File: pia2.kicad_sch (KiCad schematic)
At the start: 42 parts, among them IC25 LM393P, IC31 74LS02N, IC34 MC14050BCP, IC35 MC6821, IC9 MC6821

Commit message: move to samx4
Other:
- company: (none) -> Dragon Data
- title: (none) -> Dragon 32 CPU UK PAL
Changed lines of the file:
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@@
   (paper "A3")
   (title_block
+    (title "Dragon 32 CPU UK PAL")
     (date "2023-05-25")
     (rev "3.0")
+    (company "Dragon Data")
+    (comment 1 "Modified by Julian Brown")
+    (comment 2 "SAMx4 by Ciaran Anscomb")
   )
   (junction (at 44.45 171.45) (diameter 0) (color 0 0 0 0)

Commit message: rework board
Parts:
- removed IC35, IC9: MC6821, Package_DIP:DIP-40_W15.24mm, symbol Motorola PIA:MC6821
- removed R57: 20K 1%, Resistor_THT:R_Axial_DIN0207_L6.3mm_D2.5mm_P10.16mm_Horizontal, symbol Device:R_Small
- removed R58: 80K6 1%, Resistor_THT:R_Axial_DIN0207_L6.3mm_D2.5mm_P10.16mm_Horizontal, symbol Device:R_Small
- removed R59: 160K 1%, Resistor_THT:R_Axial_DIN0207_L6.3mm_D2.5mm_P10.16mm_Horizontal, symbol Device:R_Small
- removed R60: 330K 1%, Resistor_THT:R_Axial_DIN0207_L6.3mm_D2.5mm_P10.16mm_Horizontal, symbol Device:R_Small
- removed R61: 40K2 1%, Resistor_THT:R_Axial_DIN0207_L6.3mm_D2.5mm_P10.16mm_Horizontal, symbol Device:R_Small
- removed R62: 10K 1%, Resistor_THT:R_Axial_DIN0207_L6.3mm_D2.5mm_P10.16mm_Horizontal, symbol Device:R_Small
- removed R64: 100K, Resistor_THT:R_Axial_DIN0207_L6.3mm_D2.5mm_P10.16mm_Horizontal, symbol Device:R_Small
- added J5: 6-bit DAC, Connector_PinSocket_2.54mm:PinSocket_1x08_P2.54mm_Vertical, symbol Connector_Generic:Conn_01x08
- added U5 (x2): W65C21, Package_LCC:PLCC-44_SMD-Socket, symbol Motorola PIA:W65C21
- C2, C35, C42: footprint Capacitor_THT:CP_Radial_D5.0mm_P2.50mm -> Capacitor_SMD:CP_Elec_5x5.3
- C26, C48: footprint Capacitor_THT:C_Disc_D3.0mm_W2.0mm_P2.50mm -> Capacitor_SMD:C_0805_2012Metric_Pad1.18x1.45mm_HandSolder
- C27: footprint Capacitor_THT:C_Disc_D4.3mm_W1.9mm_P5.00mm -> Capacitor_SMD:C_0805_2012Metric_Pad1.18x1.45mm_HandSolder
- C44: footprint Capacitor_THT:C_Disc_D5.0mm_W2.5mm_P5.00mm -> Capacitor_SMD:C_0805_2012Metric_Pad1.18x1.45mm_HandSolder
- D1, D2, D3, D7: footprint Diode_THT:D_DO-35_SOD27_P7.62mm_Horizontal -> Diode_SMD:D_SOD-323_HandSoldering
- IC31: value 74LS02N -> 74ACT02; footprint Package_DIP:DIP-14_W7.62mm -> Package_SO:SOIC-14_3.9x8.7mm_P1.27mm; DigiKey 296-1627-5-ND -> MC74ACT02DR2GOSCT-ND
- IC34: value MC14050BCP -> CD4050BDR; footprint Package_DIP:DIP-16_W7.62mm -> Package_SO:SOIC-16W_7.5x10.3mm_P1.27mm; DigiKey 296-2056-ND -> 296-31503-1-ND; Note obsolete use CD4050B or convert MC14050BDG -> (none)
- R16, R32: footprint Resistor_THT:R_Axial_DIN0207_L6.3mm_D2.5mm_P2.54mm_Vertical -> Resistor_SMD:R_0805_2012Metric_Pad1.20x1.40mm_HandSolder
- R29, R38, R45, R46, R47, R48, R49, R50, R51, R52, R56, R63: footprint Resistor_THT:R_Axial_DIN0207_L6.3mm_D2.5mm_P10.16mm_Horizontal -> Resistor_SMD:R_0805_2012Metric_Pad1.20x1.40mm_HandSolder
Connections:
- net +5V: now also J5.1 (Pin_1), U5.21 (VCC), U5.21 (VCC), U5.24 (CS0), U5.24 (CS0), U5.26 (CS1), U5.26 (CS1)
- net 6bit D/A: now also J5.8 (Pin_8)
- net A0: now also U5.39 (RS0), U5.39 (RS0)
- net A1: now also U5.38 (RS1), U5.38 (RS1)
- net Alpha: now also U5.11 (PB0)
- net CART: now also U5.19 (CB1)
- net CB2: now also U5.20 (CB2)
- net CSS: now also U5.14 (PB3)
- net D0: now also U5.36 (D0), U5.36 (D0)
- net D1: now also U5.35 (D1), U5.35 (D1)
- net D2: now also U5.34 (D2), U5.34 (D2)
- net D3: now also U5.33 (D3), U5.33 (D3)
- net D4: now also U5.32 (D4), U5.32 (D4)
- net D5: now also U5.31 (D5), U5.31 (D5)
- net D6: now also U5.30 (D6), U5.30 (D6)
- net D7: now also U5.29 (D7), U5.29 (D7)
- net DAC0: now also J5.2 (Pin_2)
- net DAC1: now also J5.3 (Pin_3)
- net DAC2: now also J5.4 (Pin_4)
- net DAC3: now also J5.5 (Pin_5)
- net DAC4: now also J5.6 (Pin_6)
- net DAC5: now also J5.7 (Pin_7)
- net DC0: now also U5.3 (PA0)
- net DC1: now also U5.4 (PA1)
- net DC2: now also U5.5 (PA2)
- net DC3: now also U5.6 (PA3)
- net DC4: now also U5.7 (PA4)
- net DC5: now also U5.8 (PA5)
- net DC6: now also U5.9 (PA6)
- net DC7: now also U5.10 (PA7)
- net E: now also U5.28 (E), U5.28 (E)
- net GM0: now also U5.15 (PB4)
- net GM1: now also U5.16 (PB5)
- net GM2: now also U5.17 (PB6)
- net GND: now also U5.1 (VSS), U5.1 (VSS)
- net Inverse: now also U5.12 (PB1)
- net MEM-SIZE: now also U5.13 (PB2)
- net MOTOR: now also U5.43 (CA2)
- net P1a: now also U5.25 (~{CS2})
- net P1b: now also U5.25 (~{CS2})
- net PC0: now also U5.3 (PA0)
- net PIADAC0: now also U5.5 (PA2)
- net PIADAC1: now also U5.6 (PA3)
- net PIADAC2: now also U5.7 (PA4)
- net PIADAC3: now also U5.8 (PA5)
- net PIADAC4: now also U5.9 (PA6)
- net PIADAC5: now also U5.10 (PA7)
- net RC: now also U5.15 (PB4)
- net RClk: now also U5.14 (PB3)
- net R/~{W}: now also U5.23 (R/~{W}), U5.23 (R/~{W})
- net ~{ACK}: now also U5.44 (CA1)
- net ~{A}/G: now also U5.18 (PB7)
- net ~{BUSY}: now also U5.11 (PB0)
- net ~{FIRQ}: now also U5.41 (~{IRQB}), U5.41 (~{IRQB}), U5.42 (~{IRQA}), U5.42 (~{IRQA})
- net ~{RES}: now also U5.37 (~{RESET}), U5.37 (~{RESET})
- net ~{SelInv}: now also U5.13 (PB2)
- net at R56.2: now also U5.12 (PB1)
- net at JP2.2 (C): now also U5.4 (PA1)

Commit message: serial wiring
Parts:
- removed TR1: PN2222, Package_TO_SOT_THT:TO-92_Inline_Wide, symbol Transistor_BJT:BC141
- added TR1: PZT2222A, Package_TO_SOT_SMD:SOT-223-3_TabPin2, symbol Transistor_BJT:PZT2222A
- IC1: renamed from IC25; value LM393P -> LM393DR; footprint Package_DIP:DIP-8_W7.62mm -> Package_SO:SOP-8_3.9x4.9mm_P1.27mm; DigiKey 296-1398-5-ND -> 296-1015-1-ND
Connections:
- net Alpha: now also U5.15 (PB4); no longer U5.11 (PB0)
- net DAC1: now also IC34.12 (OUTe); no longer IC34.2 (OUTa)
- net DAC2: now also IC34.10 (OUTd); no longer IC34.4 (OUTb)
- net DAC3: now also IC34.6 (OUTc); no longer IC34.12 (OUTe)
- net DAC4: now also IC34.4 (OUTb); no longer IC34.6 (OUTc)
- net DAC5: now also IC34.2 (OUTa); no longer IC34.10 (OUTd)
- net GND: now also TR1.3 (E)
- net Inverse: now also U5.14 (PB3); no longer U5.12 (PB1)
- net PIADAC1: now also IC34.11 (INe); no longer IC34.3 (INa)
- net PIADAC2: now also IC34.9 (INd); no longer IC34.5 (INb)
- net PIADAC3: now also IC34.7 (INc); no longer IC34.11 (INe)
- net PIADAC4: now also IC34.5 (INb); no longer IC34.7 (INc)
- net PIADAC5: now also IC34.3 (INa); no longer IC34.9 (INd)
- net RC: now also U5.11 (PB0); no longer U5.15 (PB4)
- net RClk: now also U5.12 (PB1); no longer U5.14 (PB3)
- net at R32.2: now also TR1.1 (B)
- net at D1.2 (A), RL1.1: now also TR1.2 (C)

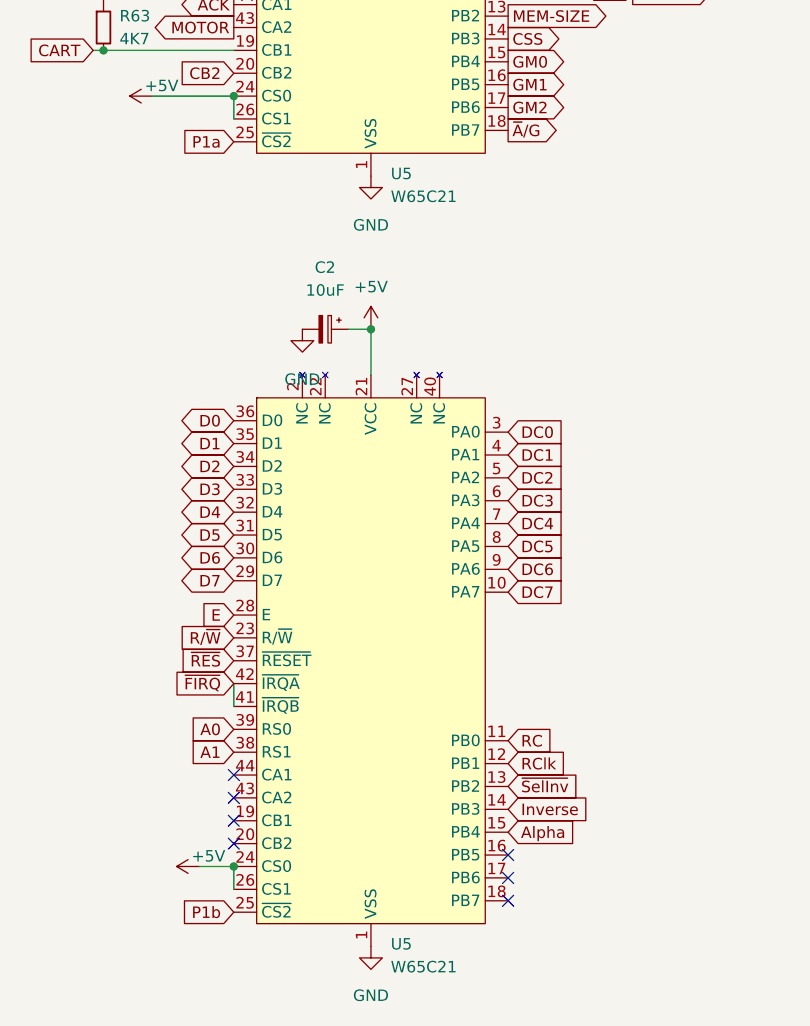
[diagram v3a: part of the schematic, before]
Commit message: fix OE timing on SRAM
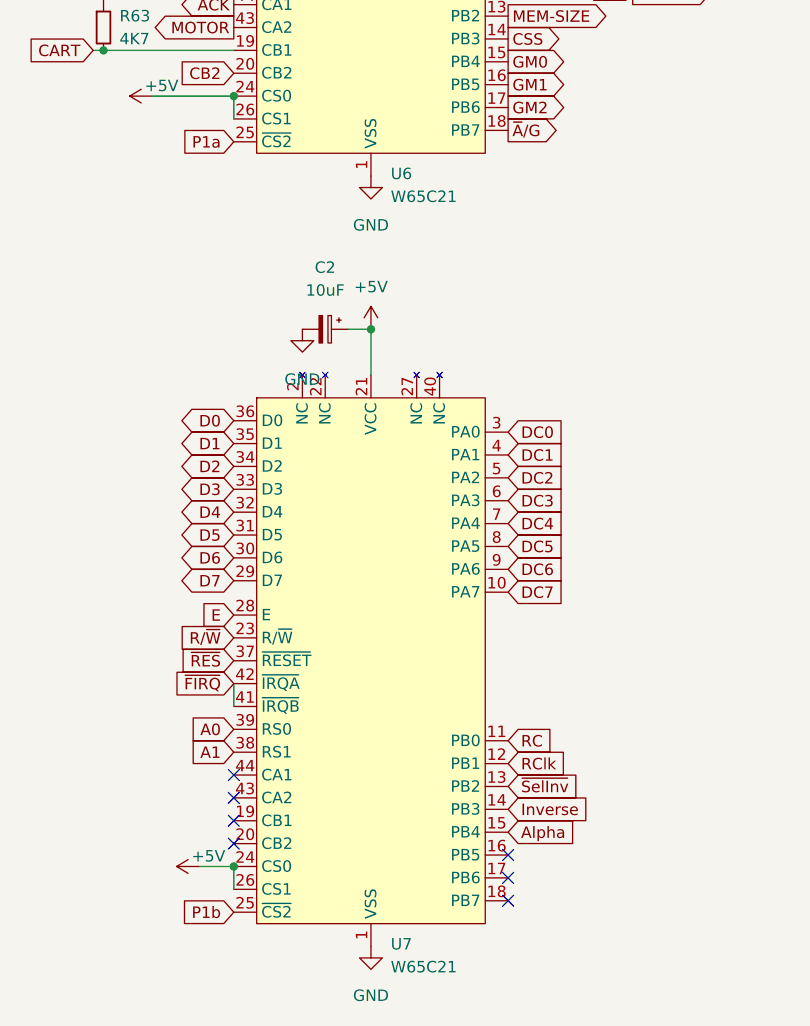
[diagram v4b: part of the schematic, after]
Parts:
- renumbered U5 to U6, U5 to U7
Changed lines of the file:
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@@
   (symbol (lib_id "Motorola PIA:W65C21") (at 59.69 64.262 0) (unit 1)
     (in_bom yes) (on_board yes) (dnp no) (fields_autoplaced)
-    (property "Reference" "U5" (at 61.8841 94.488 0)
+    (property "Reference" "U6" (at 61.8841 94.488 0)
       (effects (font (size 1.27 1.27)) (justify left))
     )
@@
     (instances
       (project "Dragon32"
-        (path "/0c3dceba-7c95-4b3d-b590-0eb581444beb/64d8d7b7-14ab-4042-9ee8-f1aec24a139c"
-          (reference "U5") (unit 1)
-        )
         (path "/0c3dceba-7c95-4b3d-b590-0eb581444beb/28dac1c2-804e-40fd-9ff5-acdb4226ab76"
           (reference "U6") (unit 1)
@@
   (symbol (lib_id "Motorola PIA:W65C21") (at 59.69 149.86 0) (unit 1)
     (in_bom yes) (on_board yes) (dnp no) (fields_autoplaced)
-    (property "Reference" "U5" (at 61.8841 180.086 0)
+    (property "Reference" "U7" (at 61.8841 180.086 0)
       (effects (font (size 1.27 1.27)) (justify left))
     )
@@
     (instances
       (project "Dragon32"
-        (path "/0c3dceba-7c95-4b3d-b590-0eb581444beb/64d8d7b7-14ab-4042-9ee8-f1aec24a139c"
-          (reference "U5") (unit 1)
-        )
         (path "/0c3dceba-7c95-4b3d-b590-0eb581444beb/28dac1c2-804e-40fd-9ff5-acdb4226ab76"
           (reference "U7") (unit 1)

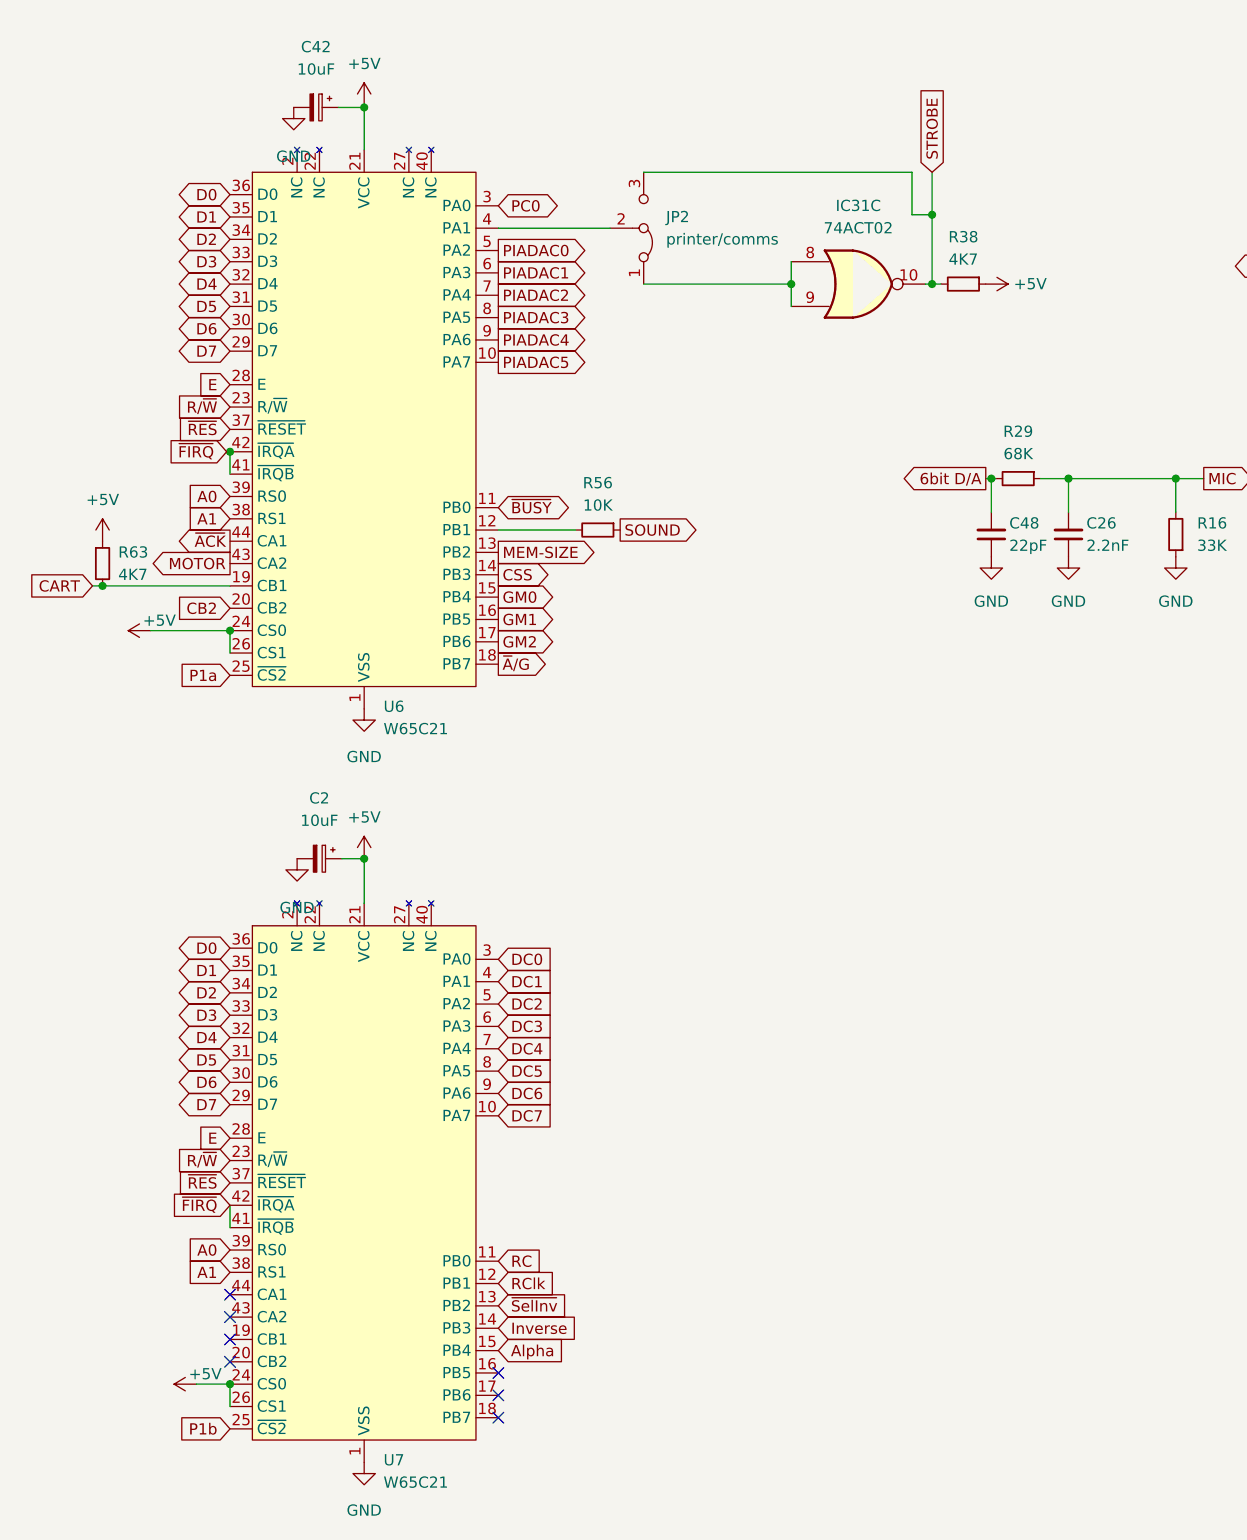
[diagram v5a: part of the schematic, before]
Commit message: switch to fpga
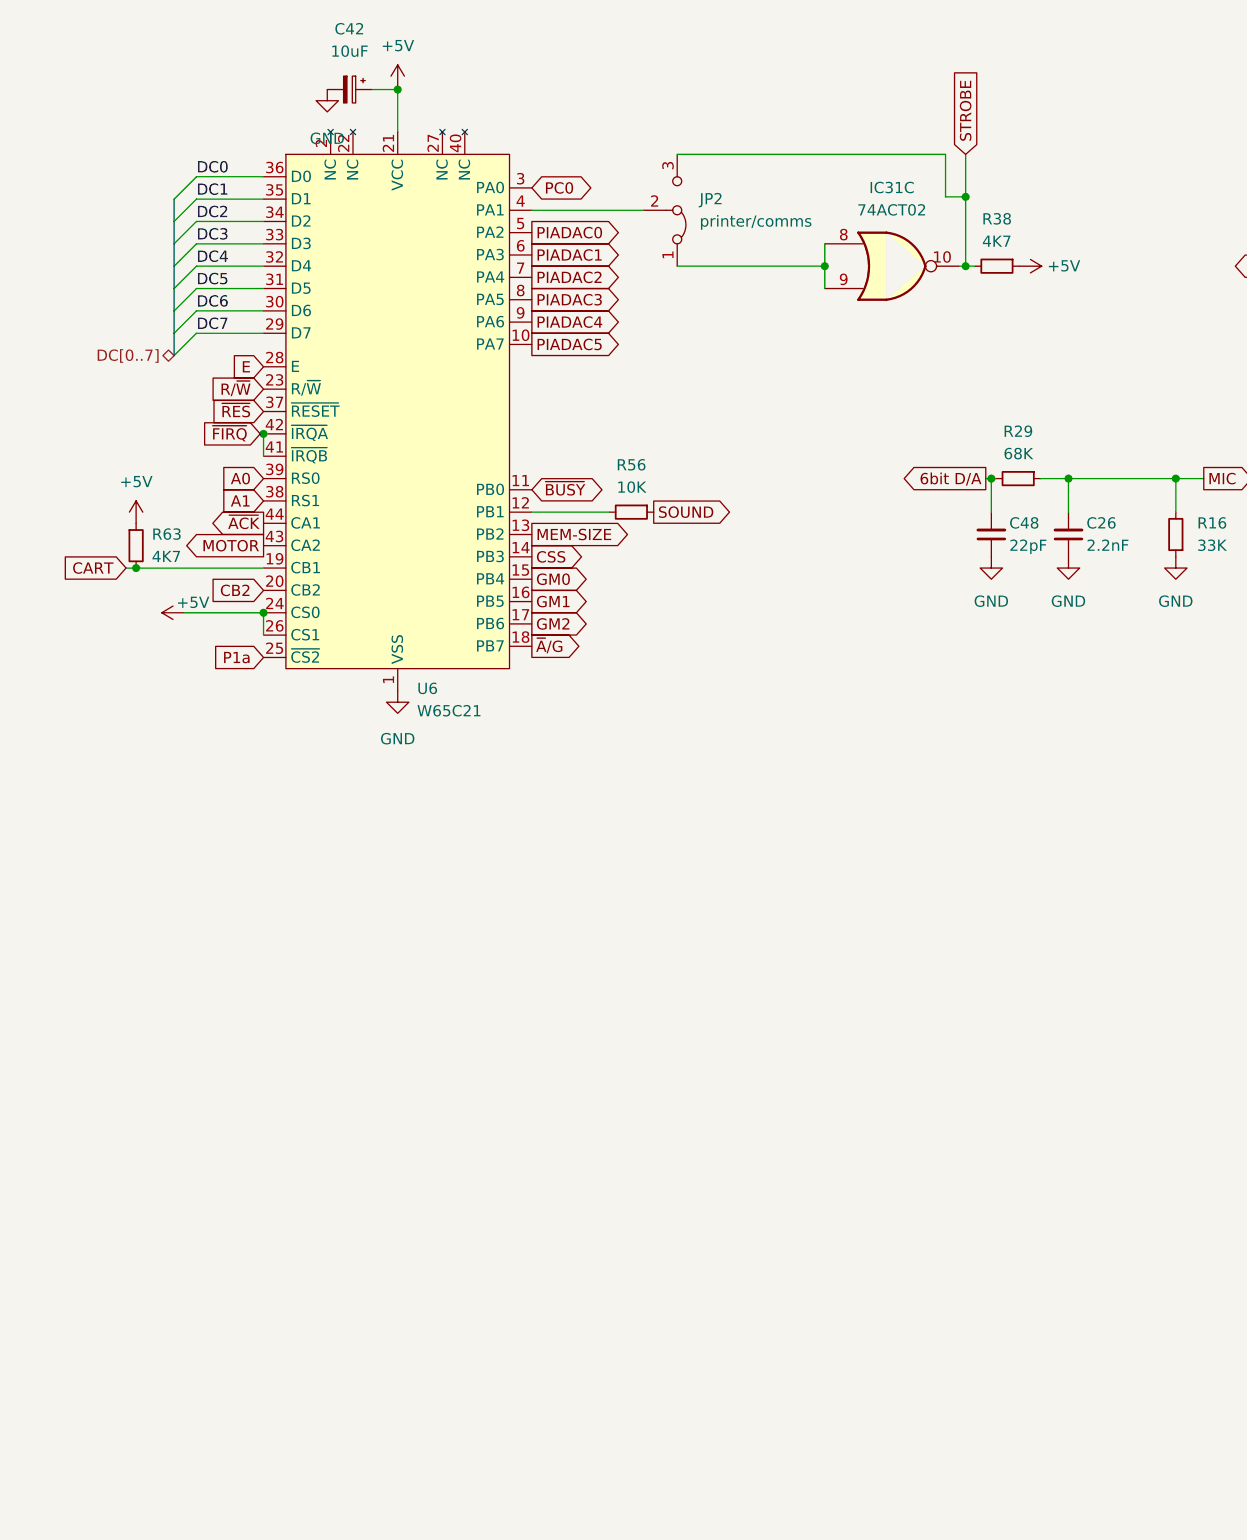
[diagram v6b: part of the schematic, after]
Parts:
- removed C2: 10uF, Capacitor_SMD:CP_Elec_5x5.3, symbol Device:C_Polarized_Small
- removed U7: W65C21, Package_LCC:PLCC-44_SMD-Socket, symbol Motorola PIA:W65C21
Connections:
- net D0 is gone; now on net DC0: U6.36 (D0)
- net D1 is gone; now on net DC1: U6.35 (D1)
- net D2 is gone; now on net DC2: U6.34 (D2)
- net D3 is gone; now on net DC3: U6.33 (D3)
- net D4 is gone; now on net DC4: U6.32 (D4)
- net D5 is gone; now on net DC5: U6.31 (D5)
- net D6 is gone; now on net DC6: U6.30 (D6)
- net D7 is gone; now on net DC7: U6.29 (D7)
- no-connect marks 8 -> 1
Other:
- moved on the sheet: C42, IC31C, JP2, R38, R56, R63, U6

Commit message: rework traces for FPGA
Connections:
- net ~{FIRQ} renamed ~{FIRQx}
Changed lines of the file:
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@@
-	)
-	(junction
-		(at 48.26 63.5)
-		(diameter 0)
-		(color 0 0 0 0)
 	)
 	(junction
@@
 		)
 	)
-	(global_label "~{FIRQ}"
-		(shape input)
-		(at 47.879 63.5 180)
-		(fields_autoplaced yes)
-		(effects
-			(font
-				(size 1.27 1.27)
-			)
-			(justify right)
-		)
-		(property "Intersheetrefs" "${INTERSHEET_REFS}"
-			(at 41.261 63.4206 0)
-			(effects
-				(font
-					(size 1.27 1.27)
-				)
-				(justify right)
-				(hide yes)
-			)
-		)
-	)
 	(global_label "PIADAC5"
 		(shape input)
@@
 				(hide yes)
 			)
+		)
+	)
+	(global_label "~{FIRQx}"
+		(shape input)
+		(at 47.879 63.5 180)
+		(fields_autoplaced yes)
+		(effects
+			(font
+				(size 1.27 1.27)
+			)
+			(justify right)
+		)
+		(property "Intersheetrefs" "${INTERSHEET_REFS}"
+			(at 40.226 63.5 0)
+			(effects
+				(font
+					(size 1.27 1.27)
+				)
+				(justify right)
+				(hide yes)
+			)
